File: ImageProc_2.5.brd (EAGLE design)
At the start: 49.8 x 23.2 mm, 117 parts, among them IC1 XC61GC3002HR-G, IC10 AT45DB642D-CNU, IC2 MIC5335-SPYMT, IC3 MIC5335-JGYMT, IC4 DSPIC33FJ128MC706A, IC5 AT86RF233-ZU, IC6 LTC6088, IC7 DRV8833RTY, IC8 DRV8833RTY, IC9 MPU-6000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

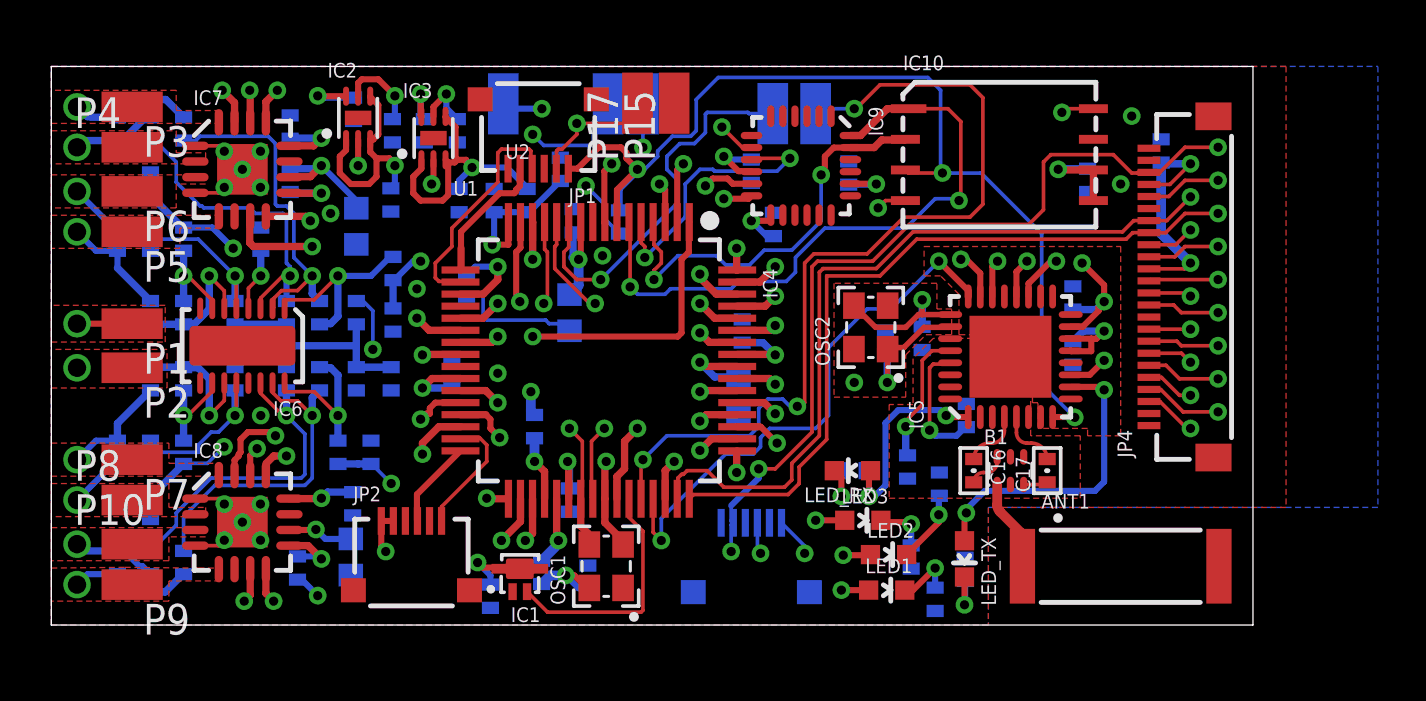
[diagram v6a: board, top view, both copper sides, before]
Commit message: ImageProc 2.5 Rev. A
Final silk screen and manufacturing modifications. Submitted for
prototype manufacturing on 7/26/2012.

ImageProc 2.5 updates the ImageProc with several new features and updated
silicon, while focusing on on enhanced manufacturability and ease of
modification. Software revisions to the octoroach and imageproc-lib codebases
are forthcoming.

Process/Manufacturing
* Changed from 2- to 4-layer process for routing and modificiation flexibility
* Functional units consolidated and rearranged for better isolation
* All ICs now on top side, (almost) all passives on bottom
* 6 mil trace/space for cheaper manufacturing processes in the prototyping
  stage
* Plane pours on all layers. Stack-up is Ground/Ground/Power/Ground. Signals
  run in all layers.
* All-new normalized part footprints, schematic symbols, and silk screen.
* Schematic now uses 5 sheets for enhanced readability. A non-free EagleCAD
  license is now required to view the files.
* A 10 mil tKeepout/bKeepout margin is now enforced at the boundaries of the
  board to ensure that the pick-and-place machine can reach all pads when the
  board is clamped into the board cradle.
* Many nets have been added and others renamed for clarification
* Much more conservative standards for component spacing

Power
* Panasonic MN13822-L voltage supervisor replaced with Torex XC61GC3002HR-G
  because the MN13822 has been discontinued
* Micrel MIC5320-JGYML 1.8/2.5 V regulator replaced with MIC5335-JGYMT
  because the MIC5320 is no longer available from suppliers.

Microcontroller
* Many pins have been relocated to make room for new features.
* Added bypass capacitors for each VDD/VSS pair and a filtering inductor
  to the VDD/AVDD connection, according to Microchip's recommendations

Radio
* ZigBee radio updated from Atmel AT86RF233 to the Atmel AT86RF233, which
  presents an identical electronic and software interface, but with silicon
  for an additional +1 dBm of transmit power
* Replaced ECS ECS-2033-160 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
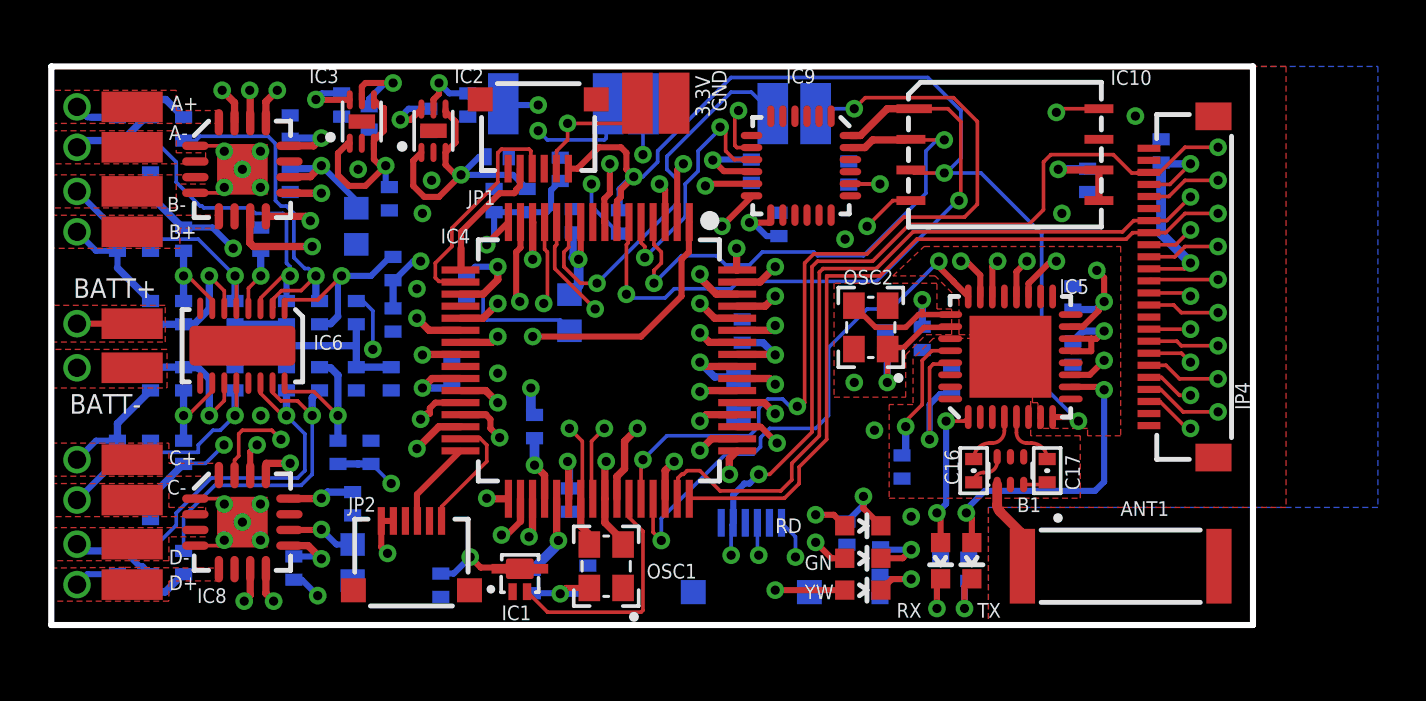
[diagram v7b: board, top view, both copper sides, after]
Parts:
- moved R7 5.47 mm to (36.9, 2.31), turned to 90 degrees
- moved LED_RX 5.23 mm to (36.9, 2.67), turned to 180 degrees
- moved C4 4.76 mm to (18.5, 19.4), turned to 0 degrees
- moved C8 3.70 mm to (13.2, 21.0)
- moved C2 3.59 mm to (12.0, 21.6)
- moved C7 3.30 mm to (17.3, 21.6)
- moved R27 3.24 mm to (34.4, 3.71)
- moved IC2 3.17 mm to (15.8, 20.5)
- moved C1 3.16 mm to (15.7, 20.9)
- moved IC3 3.05 mm to (12.9, 20.9)
- moved C5 2.90 mm to (14.0, 17.7)
- moved R28 2.85 mm to (33.0, 3.81)
- moved R26 2.35 mm to (34.4, 1.60)
- moved C3 2.11 mm to (16.2, 1.65)
- moved C20 1.50 mm to (37.3, 10.1)
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- renumbered P15 to GND, P17 to 3.3V
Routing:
- net 1.8V: track 42.1 -> 48.3 mm
- net 2.5V: track 46.2 -> 51.9 mm
- net SCK2: track 17.3 -> 22.8 mm
- net !SS1: track 28.5 -> 32.2 mm
- net !SS2_2: track 19.5 -> 22.2 mm
- net GND: track 11.2 -> 9.08 mm, vias 21 -> 23
- net N$13: track 8.33 -> 6.25 mm
- net SDI2: track 25.2 -> 27.0 mm
- net CAM_D5: track 24.4 -> 22.7 mm
- net MOTOR_C_IN1: track 36.2 -> 34.5 mm
- net IC3/INT3/RD10: track 36.4 -> 34.9 mm
- net MOTOR_D_IN1: track 34.5 -> 33.2 mm
- net 3.3V: track 64.9 -> 63.6 mm
- net CAM_D4: track 26.6 -> 25.4 mm
- net MOTOR_C_IN2: track 48.6 -> 47.5 mm
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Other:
- board text added: "2012.07.26"
- board text added: "A+"
- board text added: "A-"
- board text added: "AN1"
- board text added: "AN3"
- board text added: "AN4/IC7"
- board text added: "AN5/IC8"
- board text added: "B+"
- board text added: "B-"
- board text added: "BATT+"
- board text added: "BATT-"
- board text added: "BEARS!"
- board text added: "Biomimetic"
- board text added: "C+"
- board text added: "C-"
- board text added: "D+"
- board text added: "D-"
- board text added: "Douglas Hutchings"
- board text added: "GN"
- board text added: "GO"
- board text added: "IC3/INT3"
- board text added: "ImageProc 2.5 Rev. A"
- board text added: "Laboratory"
- board text added: "Millisystems"
- board text added: "RD"
- board text added: "RX"
- board text added: "Ryan Julian"
- board text added: "TX"
- board text added: "YW"
- board text removed: "U1"
- board text removed: "U2"
